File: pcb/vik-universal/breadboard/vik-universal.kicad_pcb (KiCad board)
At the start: 2 copper layers, 44.5 x 43 mm, 150 parts, among them J1001 Conn_01x01_Socket

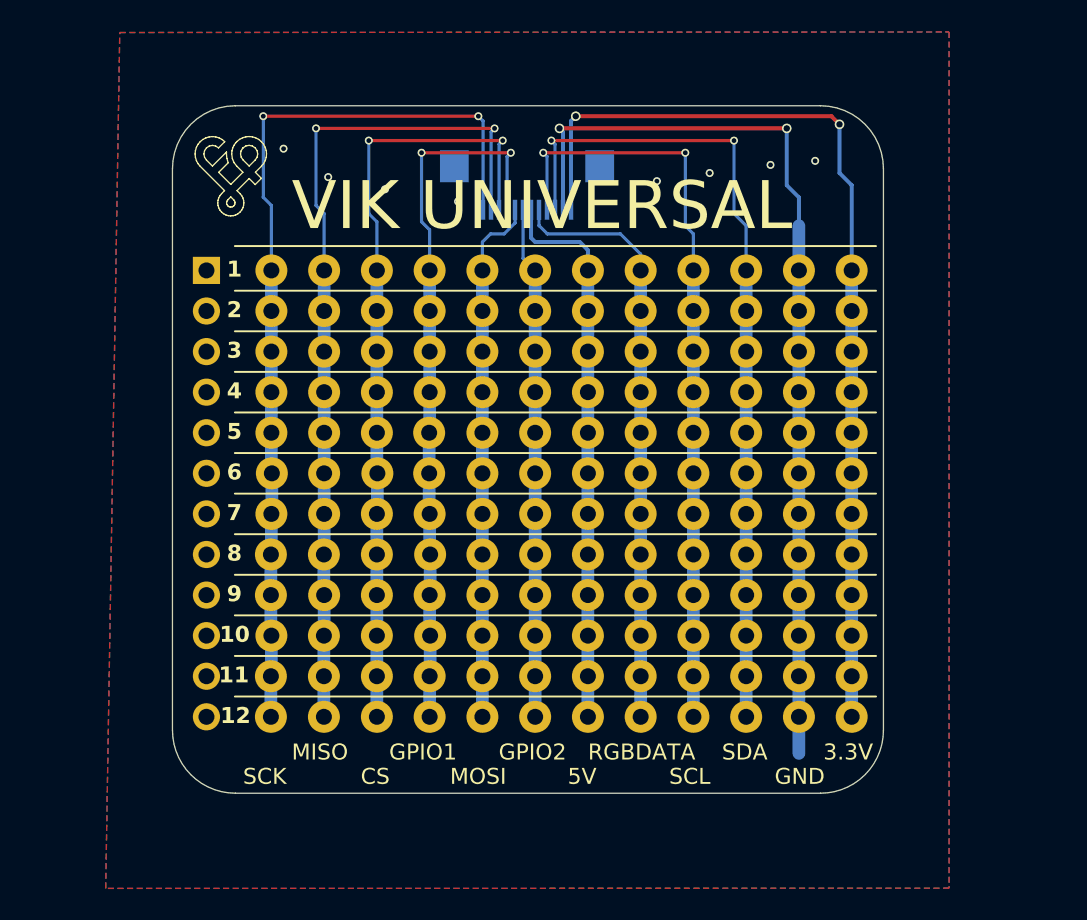
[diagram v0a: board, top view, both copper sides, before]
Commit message: Updated VIK breadboard to be 2.54mm horizontal spacing, along with a second set of numbered through holes to allow you to more easily wire up from the numbered columns to the VIK columns
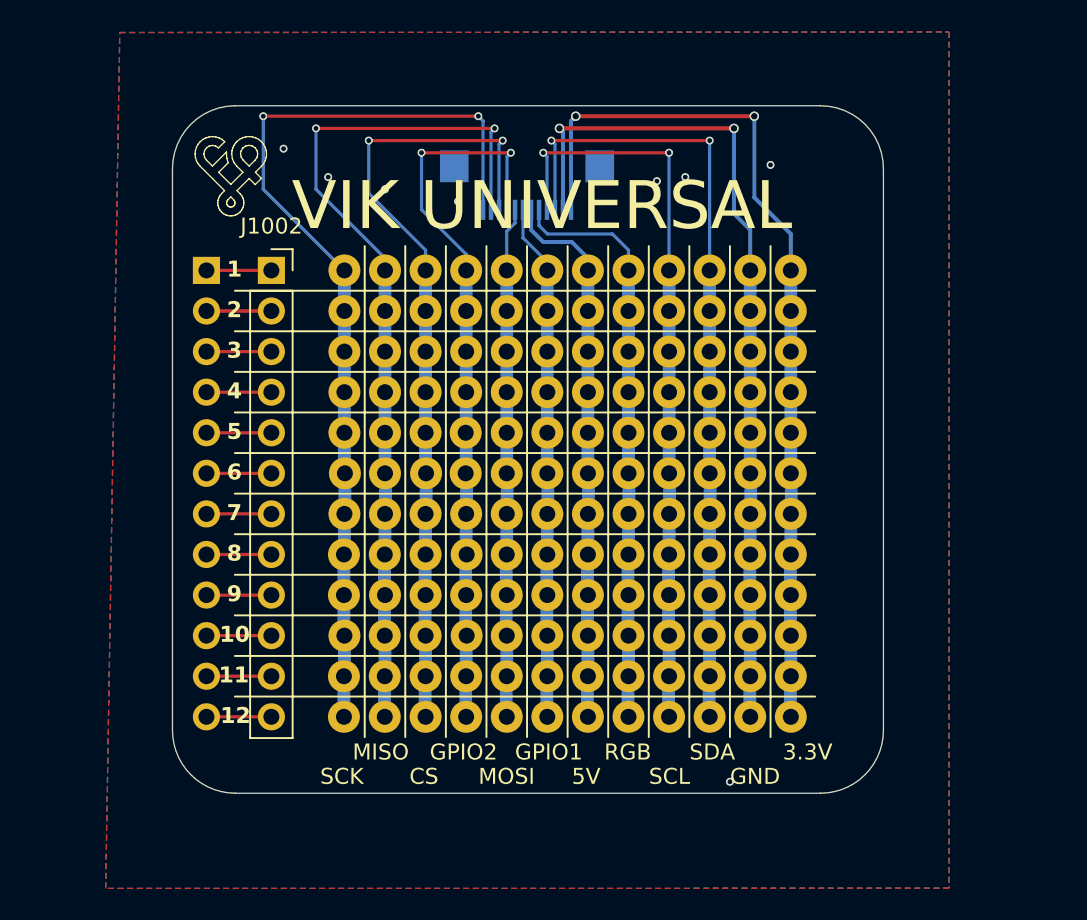
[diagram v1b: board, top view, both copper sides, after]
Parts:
- added J1002: Conn_01x01_Socket, Connector_PinSocket_2.54mm:PinSocket_1x12_P2.54mm_Vertical, F.Cu at (75.3, 96.5)
- moved JP1001 4.57 mm to (79.8, 124.5)
- moved JP1002 4.57 mm to (79.8, 121.9)
- moved JP1003 4.57 mm to (79.8, 119.4)
- moved JP1004 4.57 mm to (79.8, 116.8)
- moved JP1005 4.57 mm to (79.8, 114.3)
- moved JP1006 4.57 mm to (79.8, 111.8)
- moved JP1007 4.57 mm to (79.8, 96.5)
- moved JP1008 4.57 mm to (79.9, 109.2)
- moved JP1009 4.57 mm to (79.8, 101.6)
- moved JP1010 4.57 mm to (79.8, 99.1)
- moved JP1011 4.57 mm to (79.8, 106.7)
- moved JP1012 4.57 mm to (79.8, 104.1)
- moved JP1014 3.81 mm to (82.4, 124.5)
- moved JP1016 3.81 mm to (82.4, 114.3)
- moved JP1018 3.81 mm to (82.4, 121.9)
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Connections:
- J1001 pad 1: unconnected-(J1001-Pin_1-Pad1) -> Net-(J1001-Pin_1)
- J1001 pad 10: unconnected-(J1001-Pin_10-Pad10) -> Net-(J1001-Pin_10)
- J1001 pad 11: unconnected-(J1001-Pin_11-Pad11) -> Net-(J1001-Pin_11)
- J1001 pad 12: unconnected-(J1001-Pin_12-Pad12) -> Net-(J1001-Pin_12)
- J1001 pad 2: unconnected-(J1001-Pin_2-Pad2) -> Net-(J1001-Pin_2)
- J1001 pad 3: unconnected-(J1001-Pin_3-Pad3) -> Net-(J1001-Pin_3)
- J1001 pad 4: unconnected-(J1001-Pin_4-Pad4) -> Net-(J1001-Pin_4)
- J1001 pad 5: unconnected-(J1001-Pin_5-Pad5) -> Net-(J1001-Pin_5)
- J1001 pad 6: unconnected-(J1001-Pin_6-Pad6) -> Net-(J1001-Pin_6)
- J1001 pad 7: unconnected-(J1001-Pin_7-Pad7) -> Net-(J1001-Pin_7)
- J1001 pad 8: unconnected-(J1001-Pin_8-Pad8) -> Net-(J1001-Pin_8)
- J1001 pad 9: unconnected-(J1001-Pin_9-Pad9) -> Net-(J1001-Pin_9)
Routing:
- net GND: track 58.8 -> 53.4 mm
- net VDD_3.3V: track 60.1 -> 55.8 mm
- net Net-(J1001-Pin_9): track 0.00 -> 4.06 mm
- net Net-(J1001-Pin_8): track 0.00 -> 4.06 mm
- net Net-(J1001-Pin_7): track 0.00 -> 4.06 mm
- net Net-(J1001-Pin_6): track 0.00 -> 4.06 mm
- net Net-(J1001-Pin_5): track 0.00 -> 4.06 mm
- net Net-(J1001-Pin_4): track 0.00 -> 4.06 mm
- net Net-(J1001-Pin_3): track 0.00 -> 4.06 mm
- net Net-(J1001-Pin_2): track 0.00 -> 4.06 mm
- net Net-(J1001-Pin_12): track 0.00 -> 4.06 mm
- net Net-(J1001-Pin_11): track 0.00 -> 4.06 mm
- net Net-(J1001-Pin_10): track 0.00 -> 4.06 mm
- net Net-(J1001-Pin_1): track 0.00 -> 4.06 mm
- net SCLK: track 57.3 -> 59.2 mm
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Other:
- board text added: "RGB"
- board text removed: "RGBDATA"

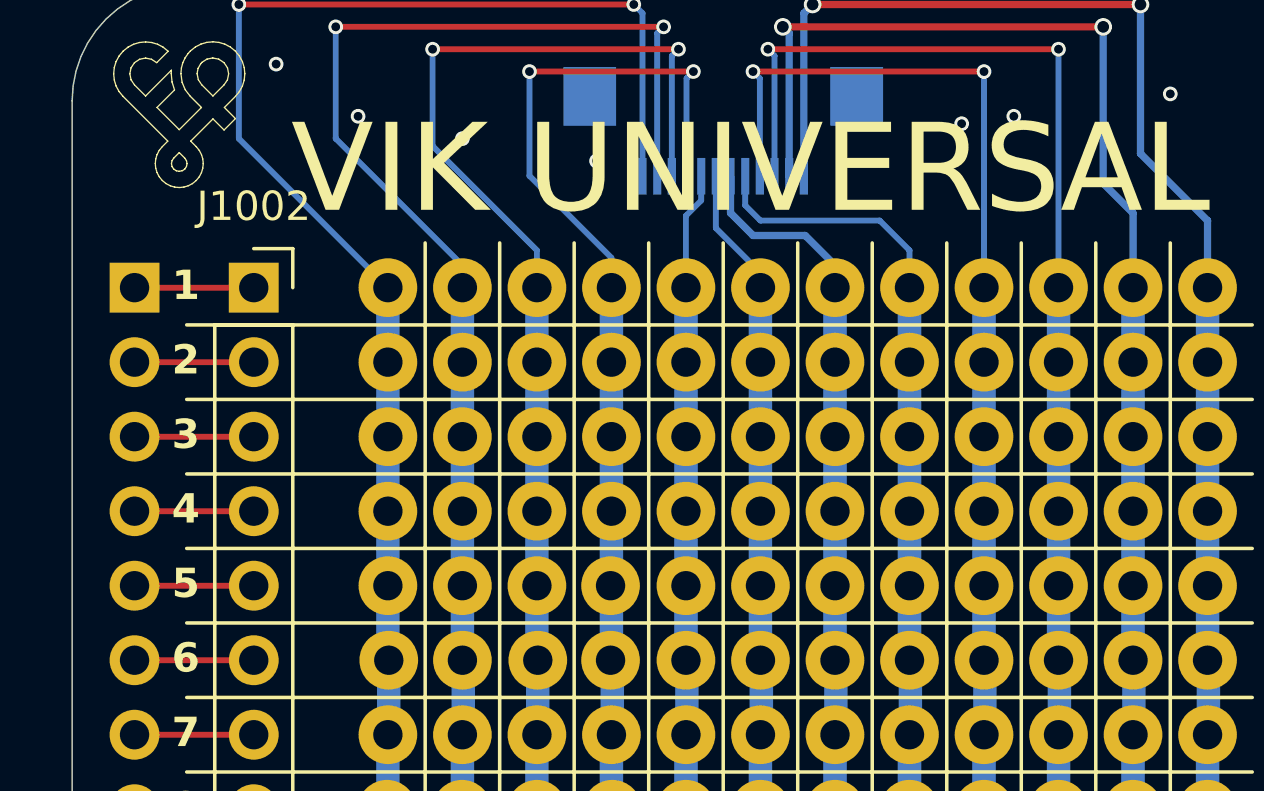
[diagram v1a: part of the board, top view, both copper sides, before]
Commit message: silkscreen adjustments for vik universal breadboard
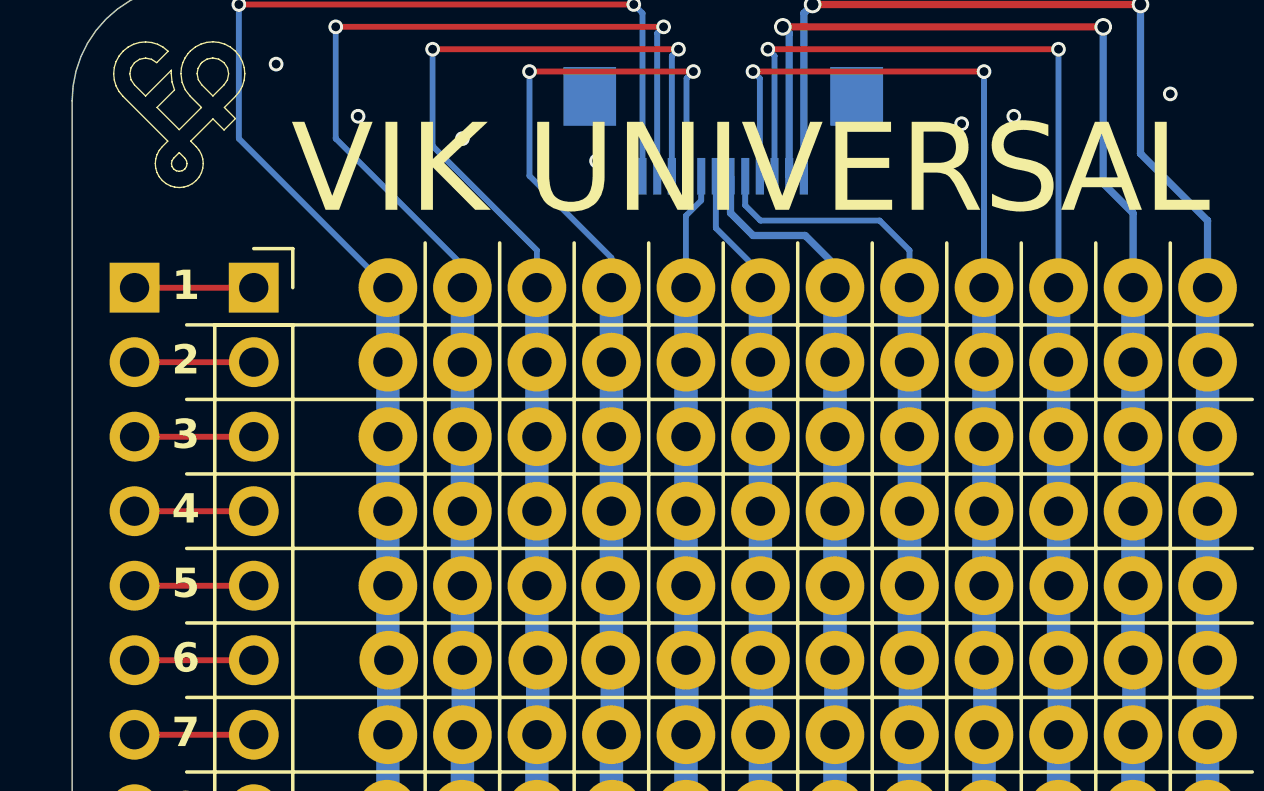
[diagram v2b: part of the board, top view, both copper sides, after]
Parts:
- moved JP1119 1.53 mm to (102.7, 106.7)
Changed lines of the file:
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@@
     (property "ki_keywords" "connector")
     (attr through_hole)
-    (fp_text reference "J1002" (at 0 -2.77) (layer "F.SilkS")
+    (fp_text reference "J1002" (at 0 -2.77) (layer "F.SilkS") hide
         (effects (font (size 1 1) (thickness 0.15)))
     )
@@
   )
   (footprint "fingerpunch:Pin_D1.0mm_L10.0mm_NoRef" (layer "B.Cu")
-    (at 101.183194 106.68 180)
+    (at 102.715694 106.68 180)
     (descr "solder Pin_ diameter 1.0mm, hole diameter 1.0mm (press fit), length 10.0mm")
     (tags "solder Pin_ press fit")
@@
     (fp_circle (center 0 0) (end 1 0)
       (stroke (width 0.12) (type solid)) (fill none) (layer "B.Fab"))
-    (pad "1" thru_hole circle (at -1.524 0 180) (size 2 2) (drill 1) (layers "*.Cu" "*.Mask")
+    (pad "1" thru_hole circle (at 0 0 180) (size 2 2) (drill 1) (layers "*.Cu" "*.Mask")
       (net 11 "SDA") (pinfunction "Pin_1") (pintype "passive"))
     (model "${KICAD6_3DMODEL_DIR}/Connector_Pin.3dshapes/Pin_D1.0mm_L10.0mm.wrl"

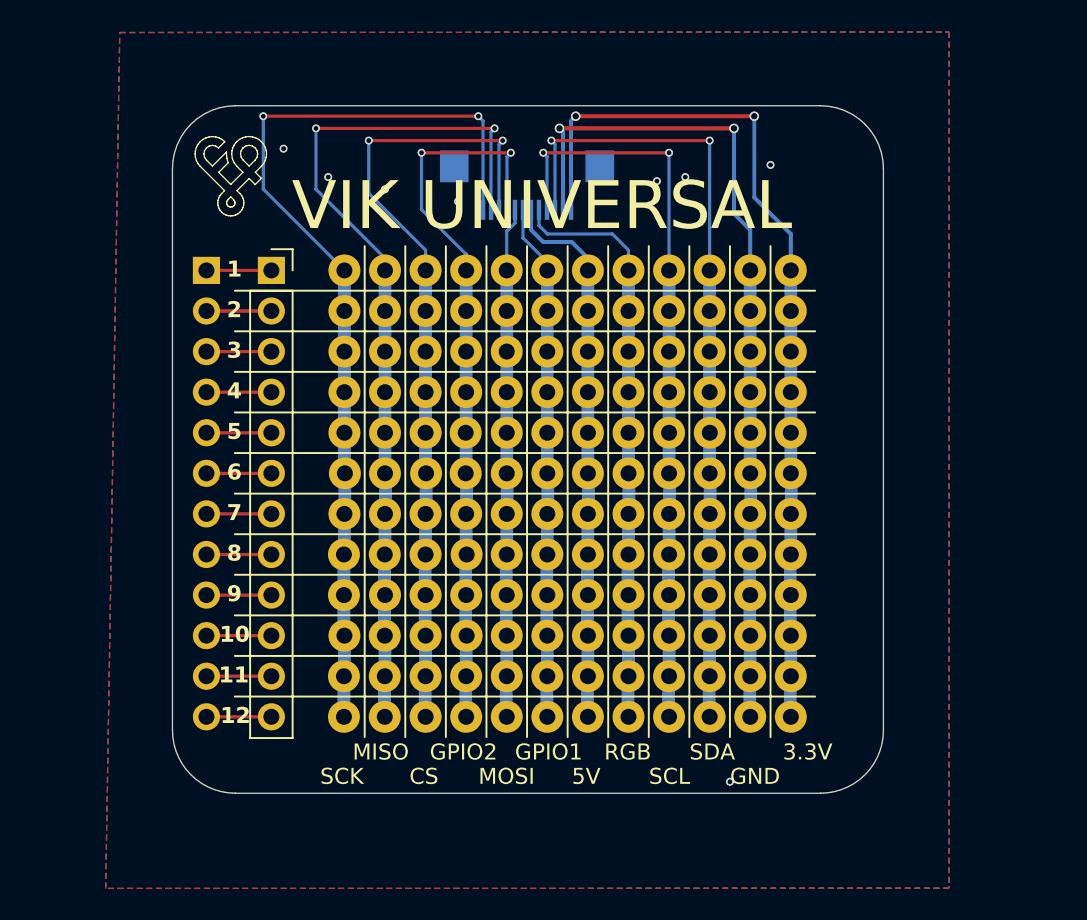
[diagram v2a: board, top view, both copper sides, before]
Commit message: realized that the vik universal breadboard wasn't actually a breadboard at all, so I redid it to be so
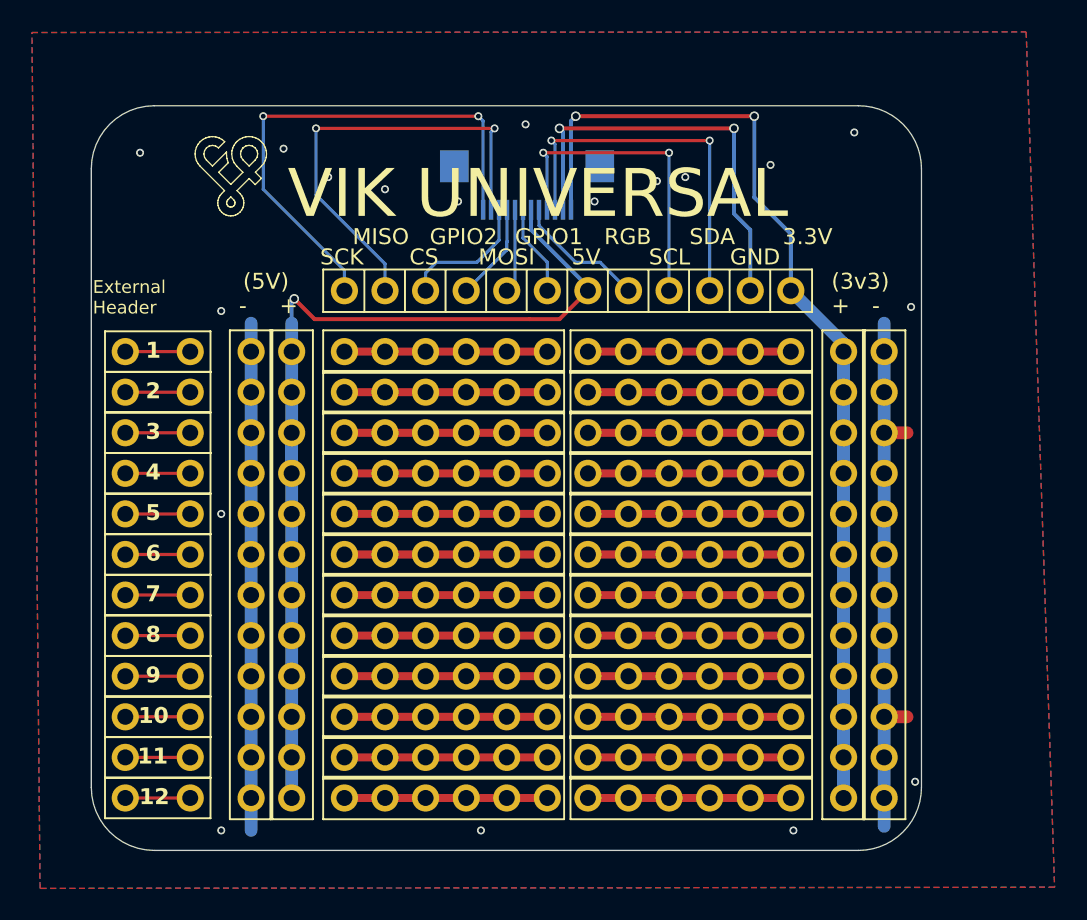
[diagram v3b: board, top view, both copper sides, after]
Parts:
- removed JP1001, JP1002, JP1003, JP1004, JP1005, JP1006, JP1007, JP1008, JP1009, JP1010, JP1011, JP1012, JP1013, JP1014, JP1015, JP1016, JP1017, JP1018, JP1019, JP1020, JP1021, JP1022, JP1023, JP1024, JP1025, JP1026, JP1027, JP1028, JP1029, JP1030, JP1031, JP1032, JP1033, JP1034, JP1035, JP1036, JP1037, JP1038, JP1039, JP1040, JP1041, JP1042, JP1043, JP1044, JP1045, JP1046, JP1047, JP1048, JP1049, JP1050, JP1051, JP1052, JP1053, JP1054, JP1055, JP1056, JP1057, JP1058, JP1059, JP1060, JP1061, JP1062, JP1063, JP1064, JP1065, JP1066, JP1067, JP1068, JP1069, JP1070, JP1071, JP1072, JP1073, JP1074, JP1075, JP1076, JP1077, JP1078, JP1079, JP1080, JP1081, JP1082, JP1083, JP1084, JP1085, JP1086, JP1087, JP1088, JP1089, JP1090, JP1091, JP1092, JP1093, JP1094, JP1095, JP1096, JP1097, JP1098, JP1099, JP1100, JP1101, JP1102, JP1103, JP1104, JP1105, JP1106, JP1107, JP1108, JP1109, JP1110, JP1111, JP1112, JP1113, JP1114, JP1115, JP1116, JP1117, JP1118, JP1119, JP1120, JP1121, JP1122, JP1123, JP1124, JP1125, JP1126, JP1127, JP1128, JP1129, JP1130, JP1131, JP1132, JP1133, JP1134, JP1135, JP1136, JP1137, JP1138, JP1139, JP1140, JP1141, JP1142, JP1143, JP1144: Conn_01x01_Socket, fingerpunch:Pin_D1.0mm_L10.0mm_NoRef
- added J1004: Conn_01x01_Socket, fingerpunch:PinSocket_1x12_P2.54mm_Vertical_IndividualSilk, F.Cu at (79.8, 97.8)
- added J1005: Conn_01x01_Socket, fingerpunch:PinSocket_1x12_P2.54mm_Vertical_6x6_SplitSilk, F.Cu at (79.8, 101.6)
- added J1006: Conn_01x01_Socket, fingerpunch:PinSocket_1x12_P2.54mm_Vertical_6x6_SplitSilk, F.Cu at (79.8, 104.1)
- added J1007: Conn_01x01_Socket, fingerpunch:PinSocket_1x12_P2.54mm_Vertical_6x6_SplitSilk, F.Cu at (79.8, 106.7)
- added J1008: Conn_01x01_Socket, fingerpunch:PinSocket_1x12_P2.54mm_Vertical_6x6_SplitSilk, F.Cu at (79.8, 109.2)
- added J1009: Conn_01x01_Socket, fingerpunch:PinSocket_1x12_P2.54mm_Vertical_6x6_SplitSilk, F.Cu at (79.8, 111.8)
- added J1010: Conn_01x01_Socket, fingerpunch:PinSocket_1x12_P2.54mm_Vertical_6x6_SplitSilk, F.Cu at (79.8, 114.3)
- added J1011: Conn_01x01_Socket, fingerpunch:PinSocket_1x12_P2.54mm_Vertical_FullSilk, F.Cu at (76.5, 101.6)
- added J1012: Conn_01x01_Socket, fingerpunch:PinSocket_1x12_P2.54mm_Vertical_6x6_SplitSilk, F.Cu at (79.8, 116.8)
- added J1013: Conn_01x01_Socket, fingerpunch:PinSocket_1x12_P2.54mm_Vertical_6x6_SplitSilk, F.Cu at (79.8, 119.4)
- added J1014: Conn_01x01_Socket, fingerpunch:PinSocket_1x12_P2.54mm_Vertical_6x6_SplitSilk, F.Cu at (79.8, 121.9)
- added J1015: Conn_01x01_Socket, fingerpunch:PinSocket_1x12_P2.54mm_Vertical_FullSilk, F.Cu at (74.0, 101.6)
- added J1016: Conn_01x01_Socket, fingerpunch:PinSocket_1x12_P2.54mm_Vertical_FullSilk, F.Cu at (111.1, 101.6)
- added J1017: Conn_01x01_Socket, fingerpunch:PinSocket_1x12_P2.54mm_Vertical_FullSilk, F.Cu at (113.6, 101.6)
- added J1018: Conn_01x01_Socket, fingerpunch:PinSocket_1x12_P2.54mm_Vertical_6x6_SplitSilk, F.Cu at (79.8, 124.5)
- added J1019: Conn_01x01_Socket, fingerpunch:PinSocket_1x12_P2.54mm_Vertical_6x6_SplitSilk, F.Cu at (79.8, 127.0)
- added J1020: Conn_01x01_Socket, fingerpunch:PinSocket_1x12_P2.54mm_Vertical_6x6_SplitSilk, F.Cu at (79.8, 129.5)
- J1001, J1002: footprint Connector_PinSocket_2.54mm:PinSocket_1x12_P2.54mm_Vertical -> fingerpunch:PinSocket_1x12_P2.54mm_Vertical_NoSilk
- moved J1001 7.18 mm to (66.1, 101.6)
- moved J1002 7.18 mm to (70.2, 101.6)
- moved ? 5.08 mm to (81.6, 103.8) (x2)
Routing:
- net CS: track 50.4 -> 8.46 mm, vias 2 -> 0
- net GPIO_AD2: track 45.8 -> 6.13 mm, vias 2 -> 0
- net GND: track 53.4 -> 92.8 mm, vias 10 -> 20
- net RGB_LED_IN: track 36.5 -> 8.28 mm
- net MOSI: track 32.0 -> 5.28 mm
- net SDA: track 50.5 -> 23.7 mm
- net SCLK: track 59.2 -> 32.5 mm
- net SCL: track 46.9 -> 20.2 mm
- net GPIO_AD1: track 32.4 -> 5.70 mm
- net MISO: track 55.0 -> 28.3 mm
- net VDD_5V: track 34.3 -> 57.5 mm, vias 0 -> 1
- net Net-(J1020-Pin_10): track 0.00 -> 12.7 mm
- net Net-(J1020-Pin_1): track 0.00 -> 12.7 mm
- net Net-(J1019-Pin_10): track 0.00 -> 12.7 mm
- net Net-(J1019-Pin_1): track 0.00 -> 12.7 mm
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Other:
- board size 44.5 x 43 mm -> 52 x 46.6 mm
- board text added: "(3v3)"
- board text added: "(5V)"
- board text added: "+"
- board text added: "-"
- board text added: "External Header"
